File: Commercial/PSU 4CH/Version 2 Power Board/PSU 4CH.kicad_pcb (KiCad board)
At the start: 2 copper layers, 37.5 x 53.3 mm, 24 parts, among them J1 I/O, J2 PSU 4CH I/O, U1 L7805, U2 LD1117-3V3, U3 TC7662, U4 LM358

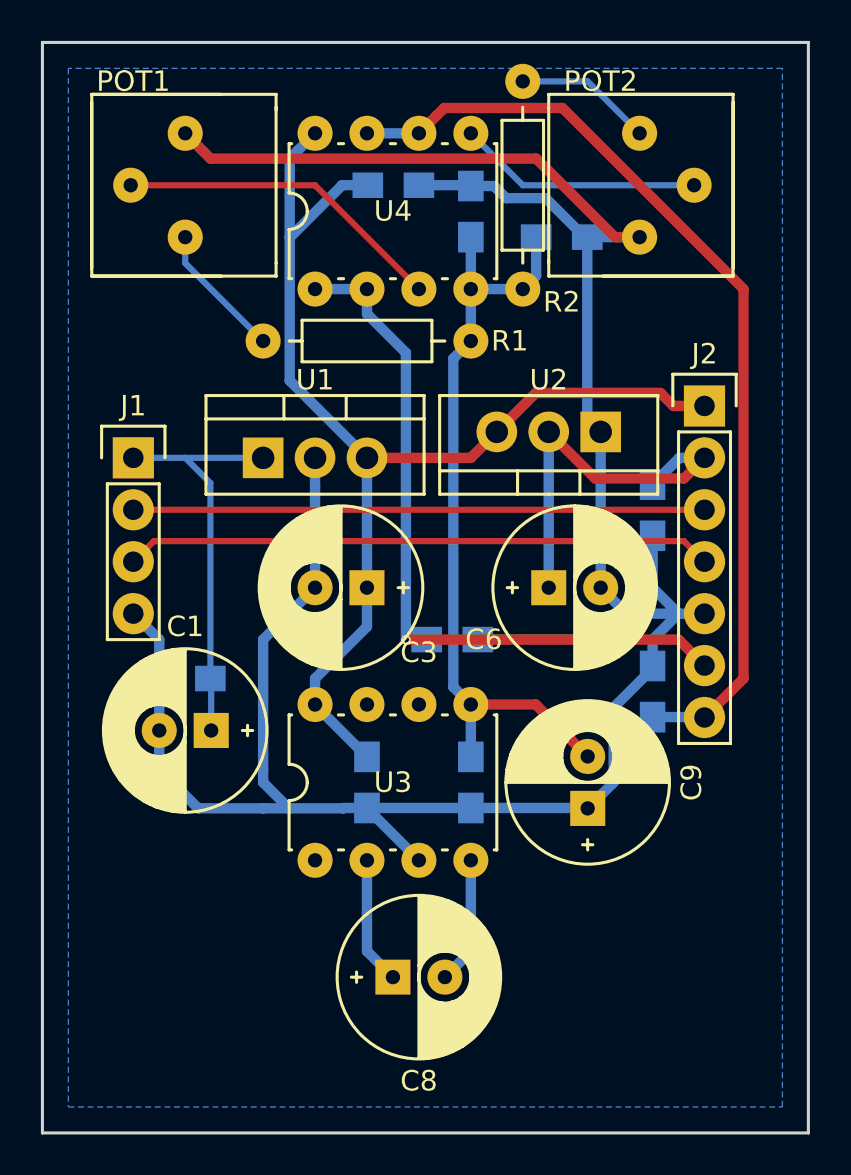
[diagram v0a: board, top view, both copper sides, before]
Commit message: PSU 4CH V2 Power Board Geber Re-generated with protel extentions
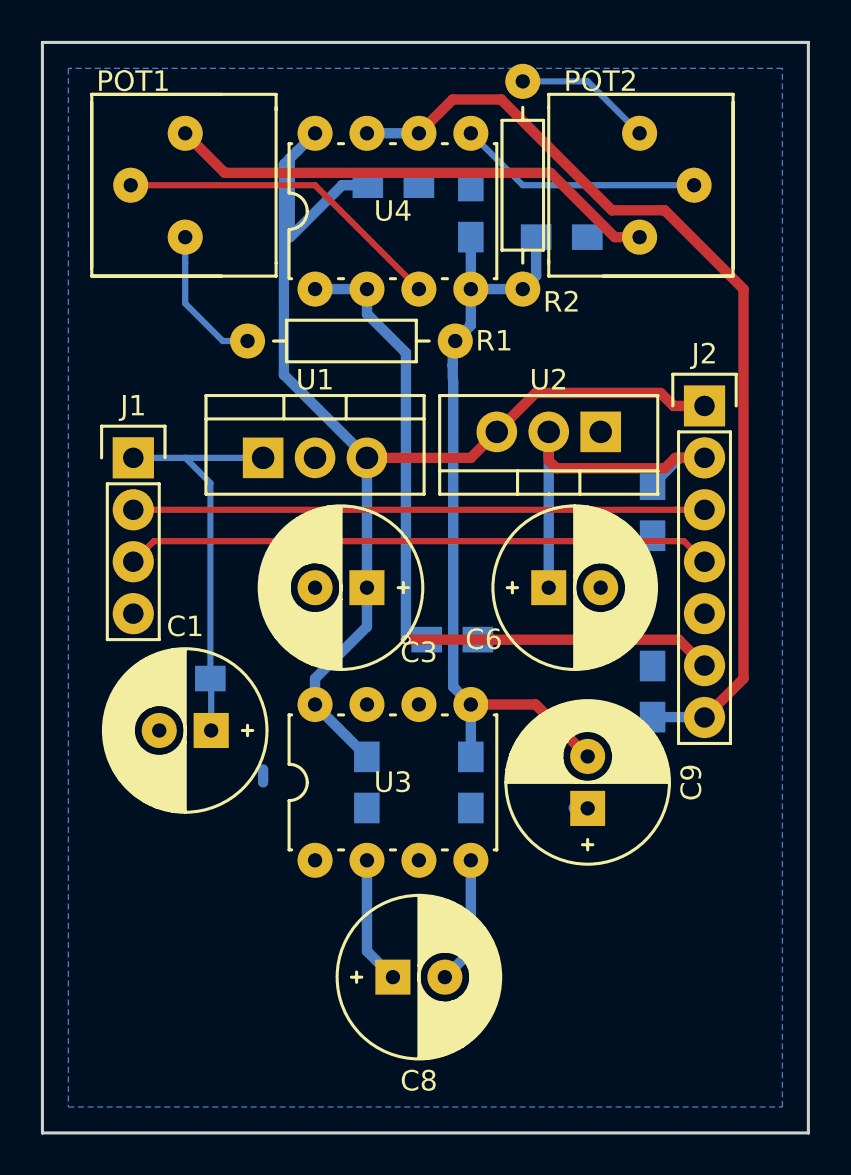
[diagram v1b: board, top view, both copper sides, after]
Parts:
- moved R1 0.76 mm to (126.9, 51.4)
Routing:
- net GND: track 134.9 -> 26.9 mm
- net +5V: track 57.6 -> 61.7 mm
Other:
- net class Default: clearance 0.127 -> 0.2
- net class Power: clearance 0.127 -> 0.2
- rule trace_clearance: 0.127 -> 0.2
